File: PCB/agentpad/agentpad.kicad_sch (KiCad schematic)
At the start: 30 parts, among them J1 Conn_01x04, SW1 SW_Push, SW10 RotaryEncoder_Switch, SW2 SW_Push, SW3 SW_Push, SW4 SW_Push, SW5 SW_Push, SW6 SW_Push, SW7 SW_Push, SW8 SW_Push, SW9 SW_Push, U1 MOUDLE-SEEEDUINO-XIAO

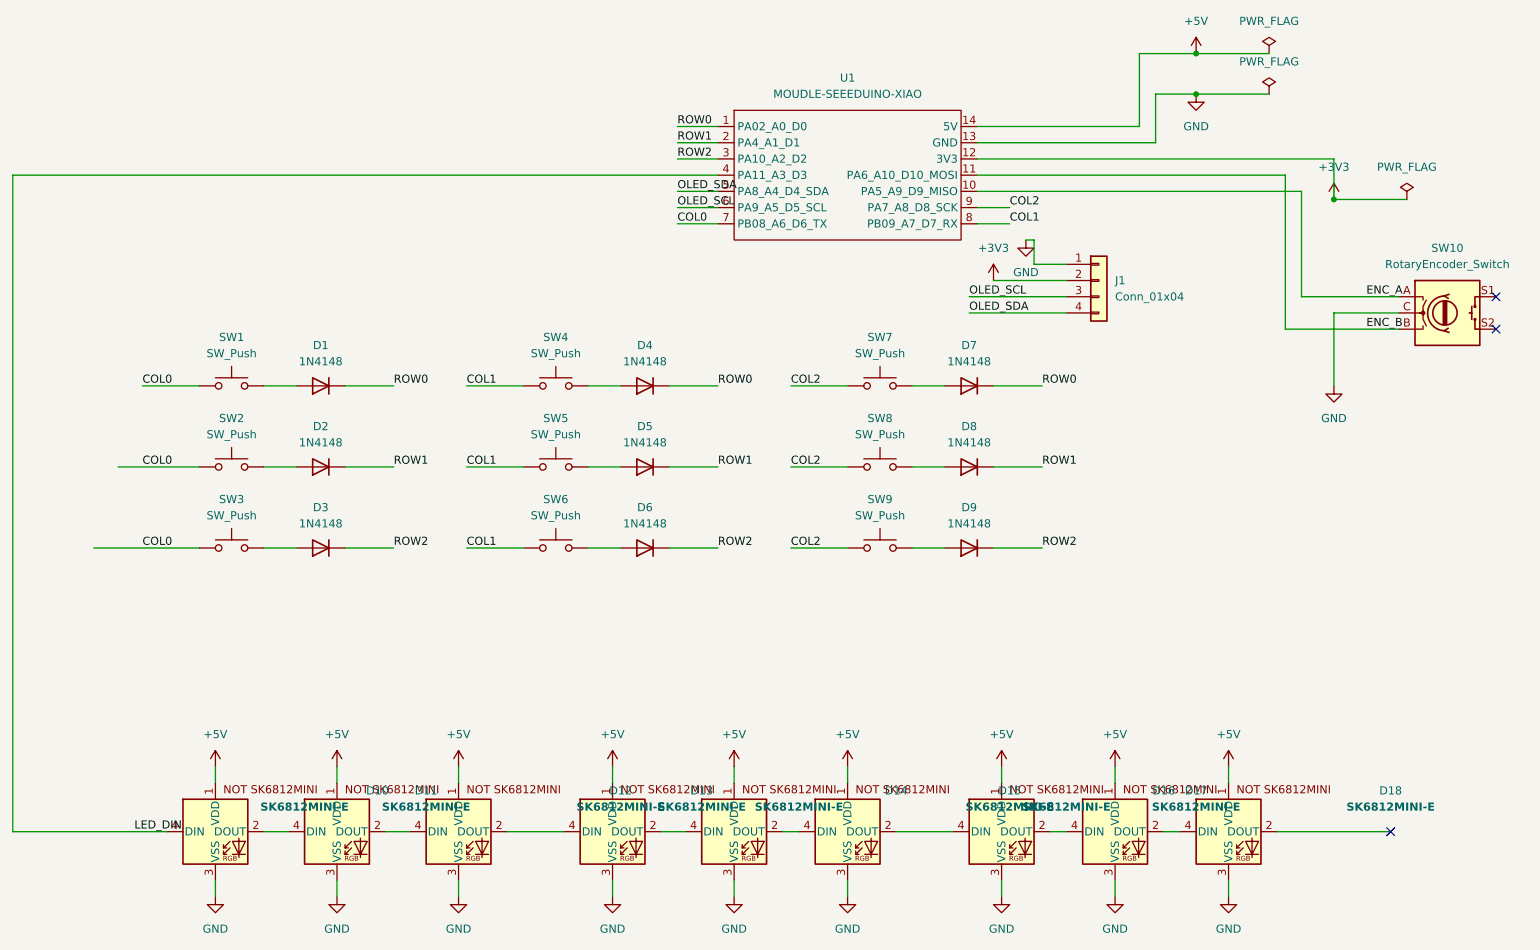
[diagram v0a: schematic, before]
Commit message: Complete v1 PCB (DRC 0 errors); drop LEDs, add gerbers.zip
9-key matrix + encoder + OLED routed on 2 layers with dual GND planes, DRC clean.
RGB deferred to v2 (SK6812 reverse-mount footprint failed edge-clearance DRC; not
required by Hackpad). Firmware + design spec + README updated to match v1.
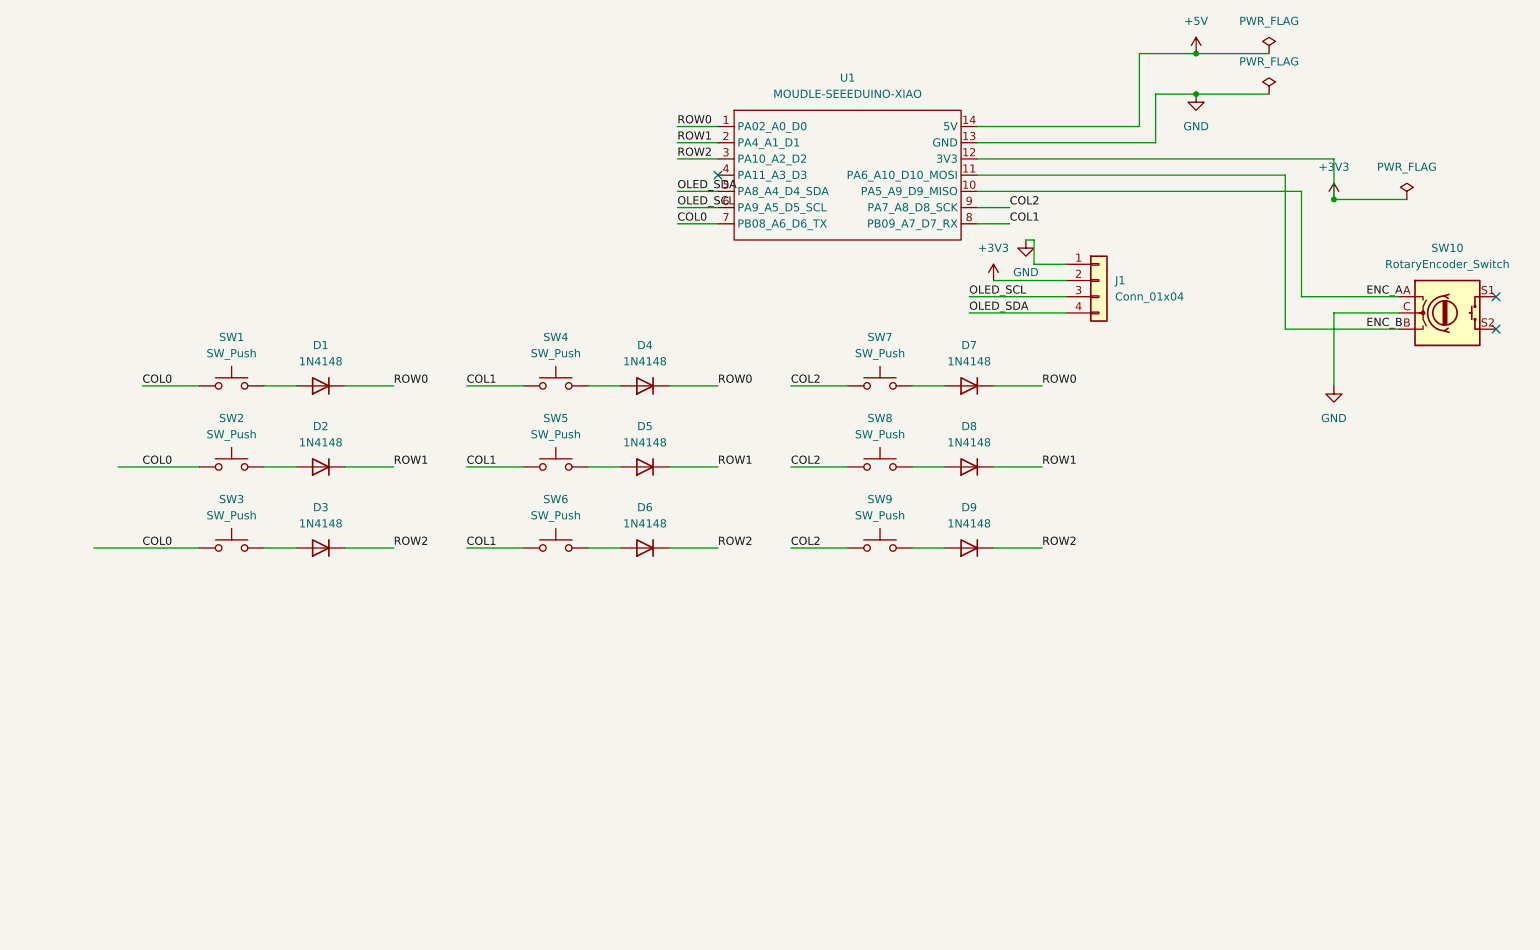
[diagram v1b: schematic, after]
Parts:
- removed D10, D11, D12, D13, D14, D15, D16, D17, D18: SK6812MINI-E, SK6812MINI-E - 3.2x2.8x1.78mm, symbol SK6812MINI-E:SK6812MINI-E
- D1, D2, D3, D4, D5, D6, D7, D8, D9: footprint (none) -> Diode_THT:D_DO-35_SOD27_P7.62mm_Horizontal
- J1: footprint (none) -> Connector_PinHeader_2.54mm:PinHeader_1x04_P2.54mm_Vertical
- SW1, SW2, SW3, SW4, SW5, SW6, SW7, SW8, SW9: footprint (none) -> Button_Switch_Keyboard:SW_Cherry_MX_1.00u_PCB
- SW10: footprint (none) -> Rotary_Encoder:RotaryEncoder_Alps_EC11E-Switch_Vertical_H20mm
- U1: footprint (none) -> hackpad:XIAO-Generic-Hybrid-14P-2.54-21X17.8MM
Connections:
- net LED_DIN: no longer names the net of U1.4 (PA11_A3_D3)
